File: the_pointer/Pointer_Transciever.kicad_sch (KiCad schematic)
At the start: 51 parts, among them J2 Conn_Coaxial, J3 BMI-S-202-F, U3 CC1101RGPR, U4 CC1190RGVR, U5 B39921B3728U410, X1 STDCRG2-27M

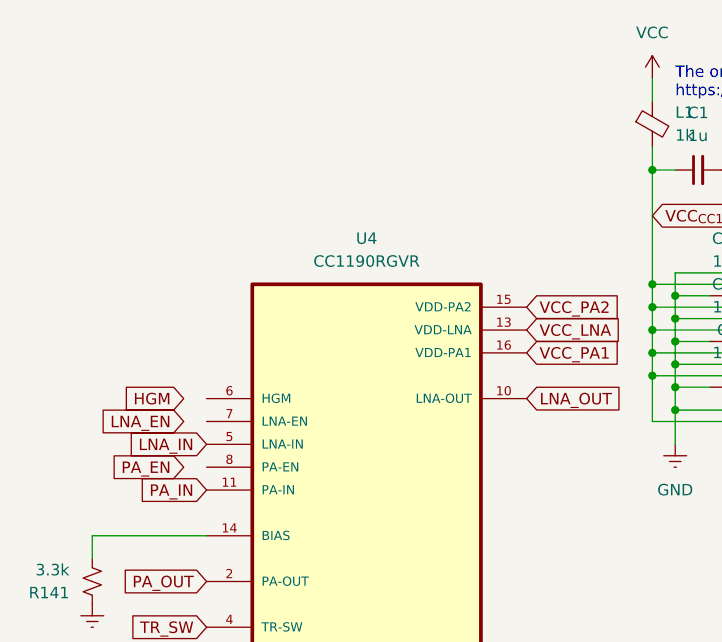
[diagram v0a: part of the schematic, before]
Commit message: Routed Pointer RF transmitter
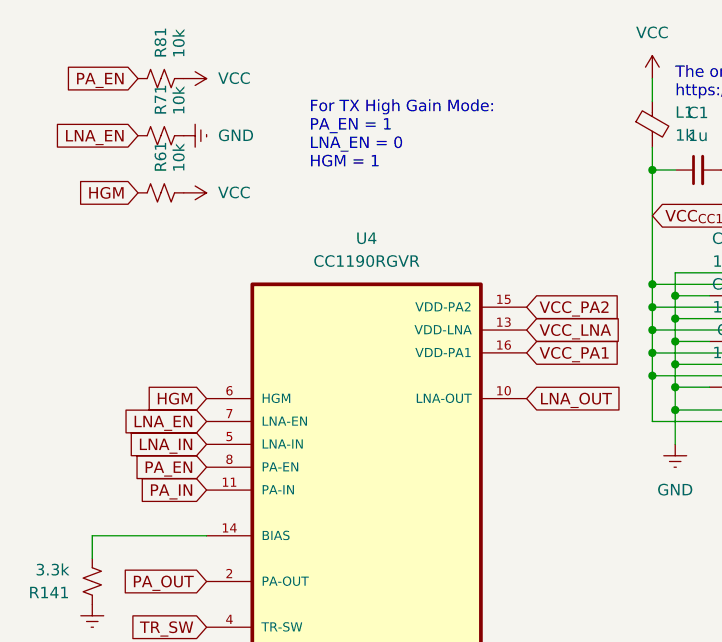
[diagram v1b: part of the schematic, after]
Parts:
- added R61, R71, R81: 10k, Resistor_SMD:R_0603_1608Metric, symbol Device:R_Small_US
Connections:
- net GND: now also R71.2
- net HGM: now also U4.6 (HGM), R61.1
- net LNA_EN: now also U4.7 (LNA-EN), R71.1
- net PA_EN: now also U4.8 (PA-EN), R81.1
- net VCC: now also R61.2, R81.2
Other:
- note added: "For TX High Gain Mode: PA_EN = 1 LNA_EN = 0 HGM = 1"
